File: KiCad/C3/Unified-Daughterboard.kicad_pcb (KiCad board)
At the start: 2 copper layers, 18 x 16.5 mm, 14 parts, among them J1 TYPE-C-31-M12_13, J2 SM04B-SRSS-TB(LF)(SN), U1 TPD4E05U06DQAR

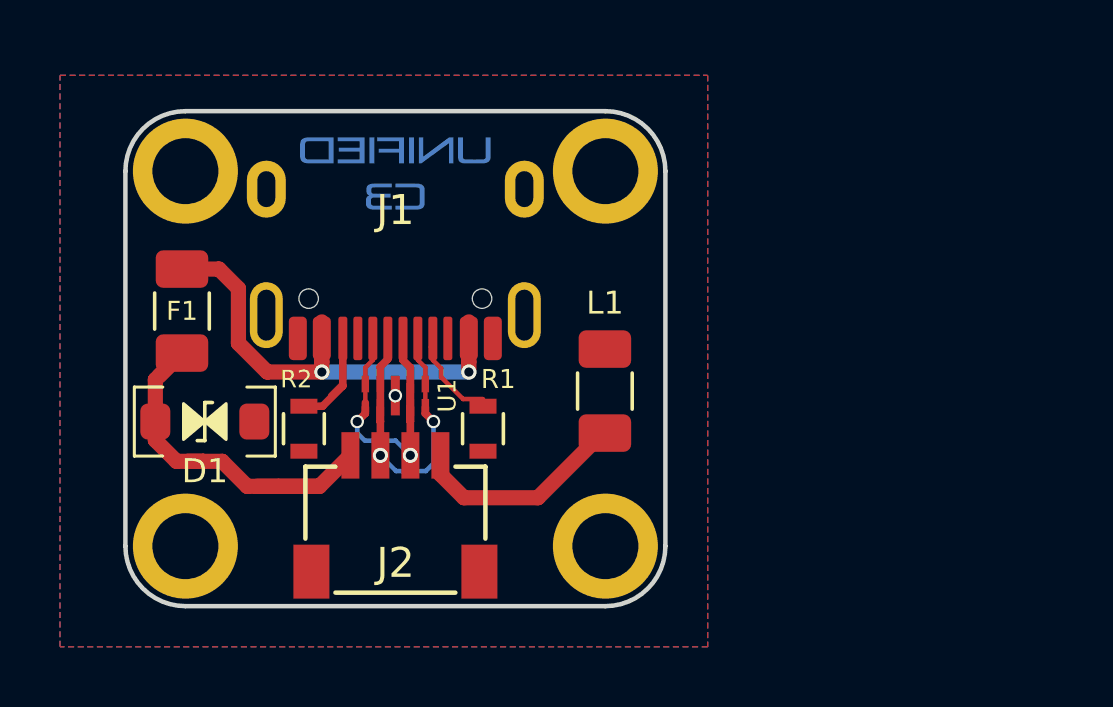
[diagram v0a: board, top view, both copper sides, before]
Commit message: Added Battery and charging management to schematic and PCB
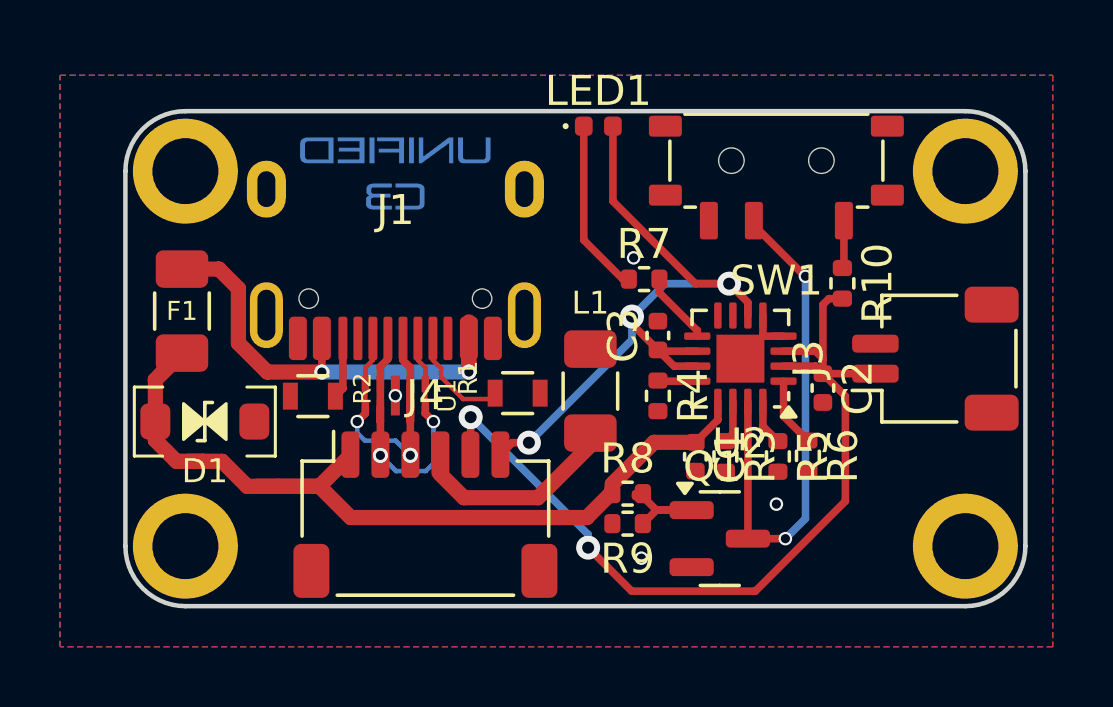
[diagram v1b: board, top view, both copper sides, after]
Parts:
- removed J2: SM04B-SRSS-TB(LF)(SN), random-keyboard-parts:JST-SR-4
- added C1: 4u7, Capacitor_SMD:C_0402_1005Metric, F.Cu at (85.0, 68.1)
- added C2: 4u7, Capacitor_SMD:C_0402_1005Metric, F.Cu at (89.3, 65.8)
- added C3: 4u7, Capacitor_SMD:C_0402_1005Metric, F.Cu at (83.8, 64.0)
- added J3: Battery, Connector_JST:JST_SH_SM02B-SRSS-TB_1x02-1MP_P1.00mm_Horizontal, F.Cu at (93.0, 64.8)
- added J4: Conn_01x06, Connector_JST:JST_SH_SM06B-SRSS-TB_1x06-1MP_P1.00mm_Horizontal, F.Cu at (76.0, 70.0)
- added LED1: orange, LED_SMD:LED_0402_1005Metric, F.Cu at (81.8, 57.0)
- added Q1: 2N7002, Package_TO_SOT_SMD:SOT-23, F.Cu at (85.8, 70.8)
- added R10: 100k, Resistor_SMD:R_0402_1005Metric, F.Cu at (89.9, 62.3)
- added R3: 47k, Resistor_SMD:R_0402_1005Metric, F.Cu at (86.0, 68.1)
- added R4: 1k5, Resistor_SMD:R_0402_1005Metric, F.Cu at (83.8, 66.0)
- added R5: 3k9, Resistor_SMD:R_0402_1005Metric, F.Cu at (87.8, 68.1)
- added R6: 10k, Resistor_SMD:R_0402_1005Metric, F.Cu at (88.8, 68.0)
- added R7: 1k5, Resistor_SMD:R_0402_1005Metric, F.Cu at (83.3, 62.1)
- added R8: 100R, Resistor_SMD:R_0402_1005Metric, F.Cu at (82.7, 69.3)
- added R9: 10k, Resistor_SMD:R_0402_1005Metric, F.Cu at (82.7, 70.3)
- added SW1: PWR, PCM_marbastlib-various:SW_MSK12C02-HB, F.Cu at (87.7, 58.2)
- added U2: BQ24075, Package_DFN_QFN:VQFN-16-1EP_3x3mm_P0.5mm_EP1.6x1.6mm, F.Cu at (86.5, 64.8)
- moved MH2 12.0 mm to (94.0, 58.5)
- moved MH4 12.0 mm to (94.0, 71.0)
- moved R1 1.66 mm to (79.1, 65.9), turned to 0 degrees
- moved R2 1.13 mm to (72.3, 66.0), turned to 180 degrees
- moved L1 0.48 mm to (81.5, 65.9)
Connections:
- J1 pad A8: Net-(J1-PadA8) -> unconnected-(J1-SBU1-PadA8)
- J1 pad B8: Net-(J1-PadB8) -> unconnected-(J1-SBU2-PadB8)
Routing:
- net +BATT: track 0.00 -> 29.8 mm, vias 0 -> 2
- net +VSW: track 0.00 -> 23.6 mm, vias 0 -> 3
- net SYSOFF: track 0.00 -> 17.5 mm, vias 0 -> 2
- net VCC: track 14.7 -> 30.6 mm
- net Net-(LED1-K): track 0.00 -> 5.84 mm
- net Net-(J1-CC2): track 6.33 -> 2.58 mm
- net Net-(Q1-G): track 0.00 -> 3.62 mm
- net GNDPWR: track 0.14 -> 2.60 mm, vias 1 -> 4
- net Net-(U2-~{CHG}): track 0.00 -> 2.42 mm
- net Net-(U2-TS): track 0.00 -> 2.32 mm
- net Net-(SW1-A): track 0.00 -> 1.74 mm
- net Net-(U2-ISET): track 0.00 -> 1.52 mm
- net /TMR: track 0.00 -> 1.42 mm
- net /ILIM: track 0.00 -> 1.32 mm
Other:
- board size 18 x 16.5 mm -> 30 x 16.5 mm
- net class Default removed
- net class Power removed
